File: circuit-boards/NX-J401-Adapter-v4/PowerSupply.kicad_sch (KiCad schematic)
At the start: 23 parts, among them Q4 CSD16322Q5, Q5 SI4483ADY-T1-GE3, U1 LM3478MA

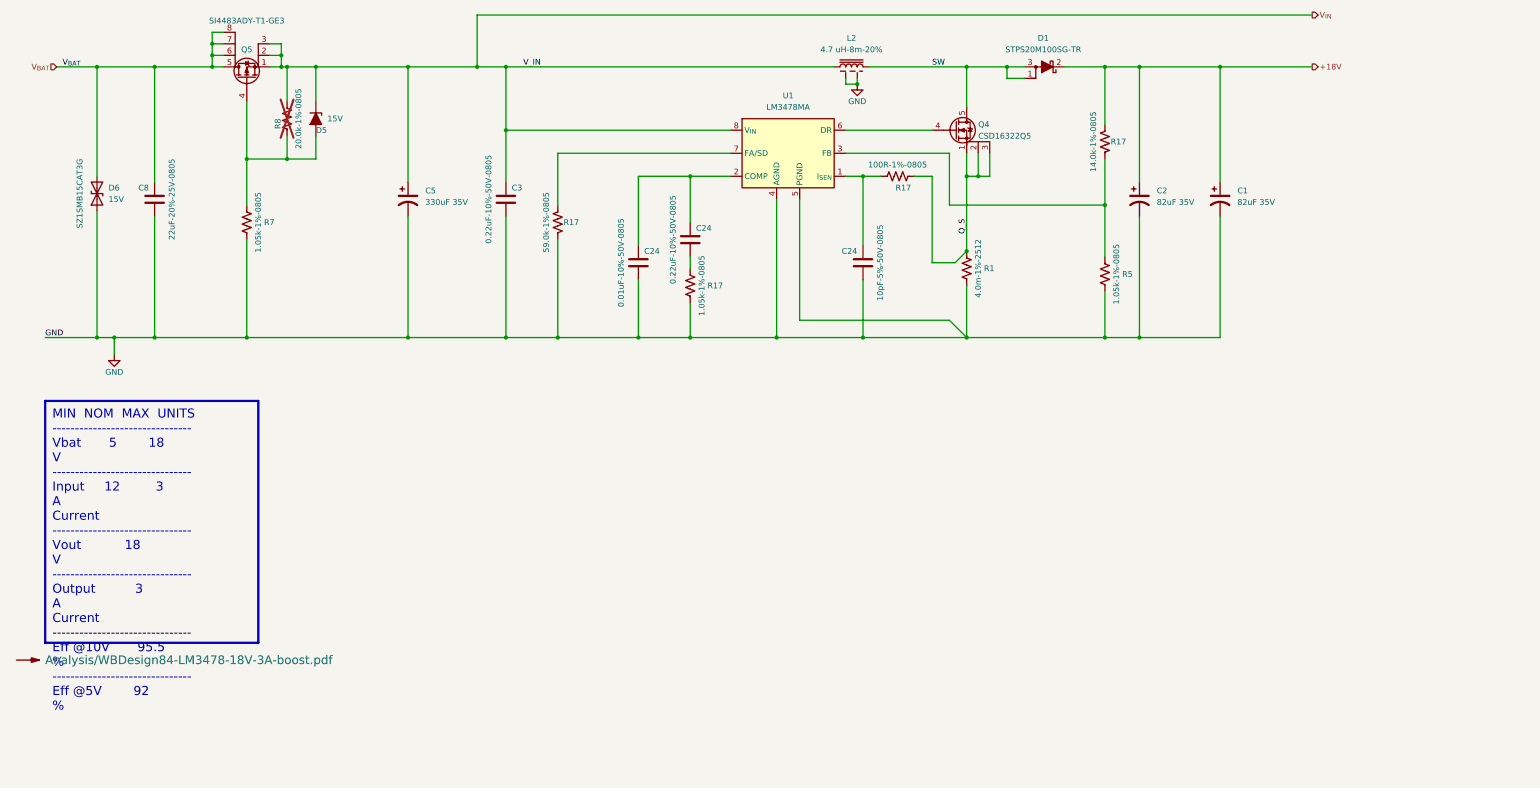
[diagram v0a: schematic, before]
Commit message: Update NX J401 Adapter to add PC LED and swap buttons
Signed-off-by: Scott Berman <sgberman1@gmail.com>
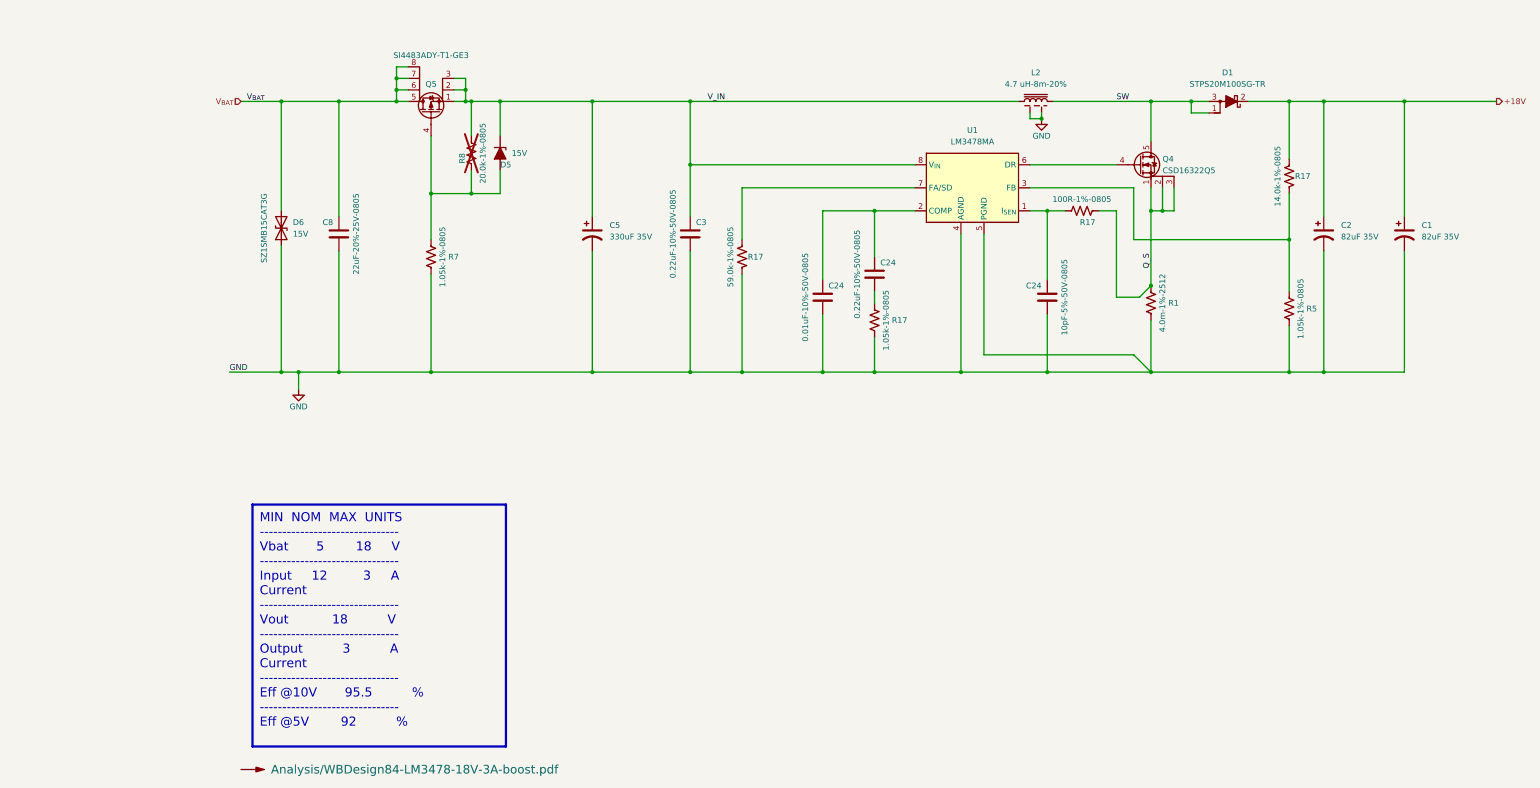
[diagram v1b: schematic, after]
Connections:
- net V_{IN} renamed V_IN
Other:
- moved on the sheet: C1, C2, C24, C3, C5, C8, D1, D5, D6, L2, Q4, Q5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
